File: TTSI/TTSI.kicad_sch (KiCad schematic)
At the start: 34 parts, among them J101 Conn_01x02_Pin, Q101 NMOS, Q102 NMOS, Q103 NMOS, Q104 PMOS, Q105 NMOS, Q106 NMOS, U101 641964-1, U102 641964-1, U103 R-78E5.0-0.5, U104 74AHC1G32, U105 641964-1, U106 74AHC1G08, U107 LM555xM, U108 641964-1

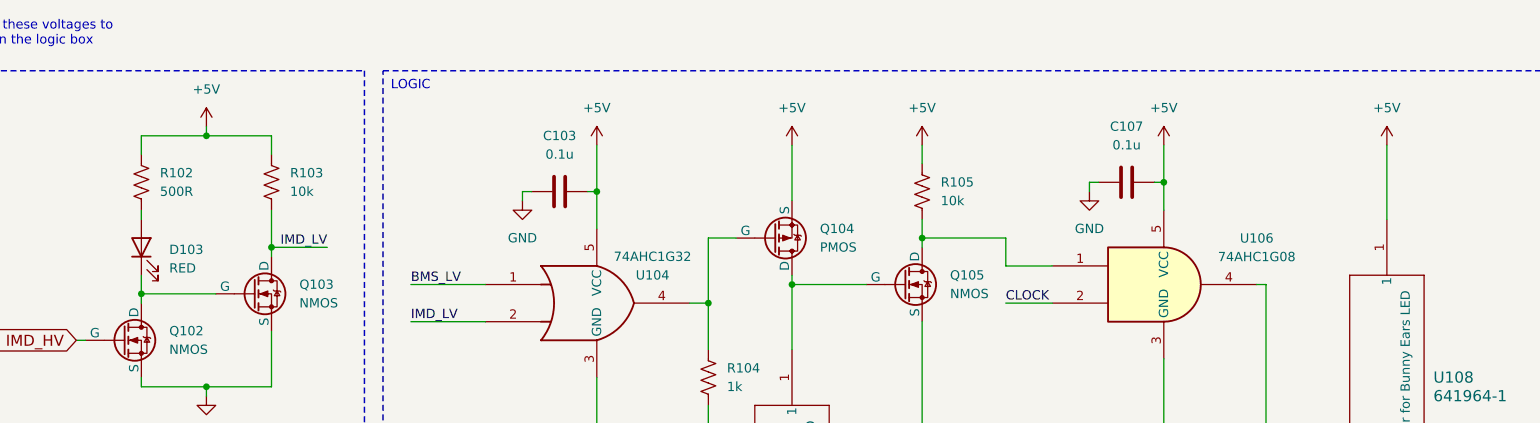
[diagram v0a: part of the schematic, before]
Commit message: Few changes to BOM as well as added 12v to bunny ears
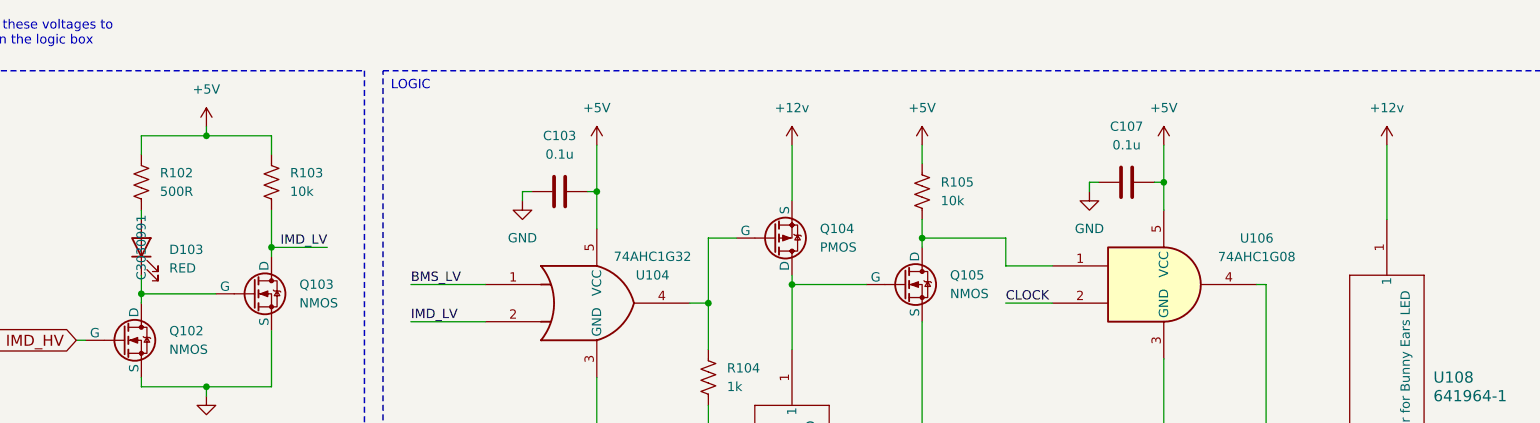
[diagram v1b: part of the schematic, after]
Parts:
- C104: footprint (none) -> Capacitor_SMD:C_0402_1005Metric
- D103: footprint (none) -> LED_SMD:LED_0201_0603Metric; JLC# (none) -> C3030991
- Q101, Q102, Q103, Q105, Q106: footprint (none) -> Package_TO_SOT_SMD:SOT-23
- Q104: footprint (none) -> Package_TO_SOT_SMD:SOT-523
- R101, R102, R103, R104, R105, R106, R107, R108: footprint (none) -> Resistor_SMD:R_0201_0603Metric
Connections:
- net +5V: no longer Q104.3 (S), U108.1
- new net +12v: Q104.3 (S), U108.1
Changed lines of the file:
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@@
 			)
 		)
-		(property "Footprint" ""
+		(property "Footprint" "Resistor_SMD:R_0201_0603Metric"
 			(at 177.546 53.594 90)
 			(effects
@@
 			)
 		)
-		(property "Footprint" ""
+		(property "Footprint" "Package_TO_SOT_SMD:SOT-23"
 			(at 129.54 71.12 0)
 			(effects
@@
 			)
 		)
-		(property "Footprint" ""
+		(property "Footprint" "Resistor_SMD:R_0201_0603Metric"
 			(at 266.446 54.864 90)
 			(effects
@@
 			)
 		)
-		(property "Footprint" ""
+		(property "Footprint" "Resistor_SMD:R_0201_0603Metric"
 			(at 318.516 124.714 90)
 			(effects
@@
 			)
 		)
-		(property "Footprint" ""
+		(property "Footprint" "Resistor_SMD:R_0201_0603Metric"
 			(at 327.914 166.116 90)
 			(effects
@@
 			)
 		)
-		(property "Footprint" ""
+		(property "Footprint" "Package_TO_SOT_SMD:SOT-23"
 			(at 161.29 72.39 0)
 			(effects
@@
 			)
 		)
-		(property "Datasheet" "641964-1"
+		(property "Datasheet" "https://www.te.com/usa-en/product-641964-1.datasheet.pdf"
 			(at 328.93 58.42 0)
 			(effects
@@
 			)
 		)
-		(property "Datasheet" "641964-1"
+		(property "Datasheet" "https://www.te.com/usa-en/product-641964-1.datasheet.pdf"
 			(at 247.65 76.2 0)
 			(effects
@@
 			)
 		)
-		(property "Footprint" ""
+		(property "Footprint" "Package_TO_SOT_SMD:SOT-23"
 			(at 331.47 118.11 0)
 			(effects
@@
 			)
 		)
-		(property "Value" "+5V"
+		(property "Value" "+12v"
 			(at 328.93 43.18 0)
 			(effects
@@
 			)
 		)
-		(property "Footprint" ""
+		(property "Footprint" "Package_TO_SOT_SMD:SOT-523"
 			(at 250.19 63.5 0)
 			(effects
@@
 			)
 		)
-		(property "Footprint" ""
+		(property "Footprint" "Resistor_SMD:R_0201_0603Metric"
 			(at 128.016 58.674 90)
 			(effects
@@
 			)
 		)
-		(property "Footprint" ""
+		(property "Footprint" "Resistor_SMD:R_0201_0603Metric"
 			(at 159.766 53.594 90)
 			(effects
@@
 			)
 		)
-		(property "Footprint" ""
+		(property "Footprint" "Capacitor_SMD:C_0402_1005Metric"
 			(at 278.13 163.83 0)
 			(effects
@@
 			)
 		)
-		(property "Footprint" ""
+		(property "Footprint" "Resistor_SMD:R_0201_0603Metric"
 			(at 237.236 80.264 90)
 			(effects
@@
 			)
 		)
-		(property "Footprint" ""
+		(property "Footprint" "Package_TO_SOT_SMD:SOT-23"
 			(at 179.07 66.04 0)
 			(effects
@@
 			)
 		)
-		(property "Datasheet" "641964-1"
+		(property "Datasheet" "https://www.te.com/usa-en/product-641964-1.datasheet.pdf"
 			(at 30.48 111.76 0)
 			(effects
@@
 			)
 		)
-		(property "Footprint" ""
+		(property "Footprint" "LED_SMD:LED_0201_0603Metric"
 			(at 158.75 62.23 0)
 			(effects
@@
 			)
 		)
-		(property "Datasheet" "~"
+		(property "Datasheet" "https://www.we-online.com/components/products/datasheet/150060RS75000.pdf"
 			(at 158.75 62.23 0)
 			(effects
@@
 			)
 		)
+		(property "JLC#" "C3030991"
+			(at 158.75 62.23 0)
+			(effects
+				(font
+					(size 1.27 1.27)
+				)
+			)
+		)
 		(pin "2"
 		)
@@
 			)
 		)
-		(property "Datasheet" "641964-1"
+		(property "Datasheet" "https://www.te.com/usa-en/product-641964-1.datasheet.pdf"
 			(at 54.61 111.76 0)
 			(effects
@@
 			)
 		)
-		(property "Footprint" ""
+		(property "Footprint" "Package_TO_SOT_SMD:SOT-23"
 			(at 267.97 64.77 0)
 			(effects
@@
 			)
 		)
-		(property "Footprint" ""
+		(property "Footprint" "Resistor_SMD:R_0201_0603Metric"
 			(at 338.074 180.086 90)
 			(effects
@@
 			)
 		)
-		(property "Value" "+5V"
+		(property "Value" "+12v"
 			(at 247.65 43.18 0)
 			(effects

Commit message: R,C values for 555. Layout start
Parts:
- C108: value C -> 22u
- R107: value R_US -> 15k
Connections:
- net +12v: no longer U108.1
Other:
- note added: "Parth 3/21/2025 -Chose values of to make 555 timer at 5Hz. -Removed 12V flag on the bunny ear LED connector after logic gate. Will connect 12V to led directly from harness for now."
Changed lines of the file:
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@@
 		)
 	)
+	(text "Parth 3/21/2025\n-Chose values of  to make 555 timer at 5Hz. \n-Removed 12V flag on the bunny ear LED connector after logic gate. \n	Will connect 12V to led directly from harness for now. \n\n"
+		(exclude_from_sim no)
+		(at 370.332 57.658 0)
+		(effects
+			(font
+				(size 2.54 2.54)
+			)
+			(justify left top)
+		)
+	)
 	(text "Ok these level shifters are shifting these voltages to \n5v for the OR GATE logic seen in the logic box\n"
 		(exclude_from_sim no)
@@
 		)
 	)
-	(text_box "ASTALE 555 - 50% DUTY - 2-5Hz"
+	(text_box "ASTABLE 555 - 50% DUTY - 2-5Hz"
 		(exclude_from_sim no)
 		(at 274.32 143.51 0)
@@
 			)
 		)
-		(property "Value" "R_US"
+		(property "Value" "15k"
 			(at 334.01 166.37 90)
 			(effects
@@
 	)
 	(symbol
-		(lib_name "+5V_1")
-		(lib_id "power:+5V")
-		(at 328.93 48.26 0)
-		(unit 1)
-		(exclude_from_sim no)
-		(in_bom yes)
-		(on_board yes)
-		(dnp no)
-		(fields_autoplaced yes)
-		(property "Reference" "#PWR0127"
-			(at 328.93 52.07 0)
-			(effects
-				(font
-					(size 1.27 1.27)
-				)
-				(hide yes)
-			)
-		)
-		(property "Value" "+12v"
-			(at 328.93 43.18 0)
-			(effects
-				(font
-					(size 1.27 1.27)
-				)
-			)
-		)
-		(property "Footprint" ""
-			(at 328.93 48.26 0)
-			(effects
-				(font
-					(size 1.27 1.27)
-				)
-				(hide yes)
-			)
-		)
-		(property "Datasheet" ""
-			(at 328.93 48.26 0)
-			(effects
-				(font
-					(size 1.27 1.27)
-				)
-				(hide yes)
-			)
-		)
-		(property "Description" "Power symbol creates a global label with name \"+5V\""
-			(at 328.93 48.26 0)
-			(effects
-				(font
-					(size 1.27 1.27)
-				)
-				(hide yes)
-			)
-		)
-		(pin "1"
-		)
-		(instances
-			(project "TTSI 4"
-				(path "/8333e4c5-977f-459c-982e-d2d7d024e7e8"
-					(reference "#PWR0127")
-					(unit 1)
-				)
-			)
-		)
-	)
-	(symbol
 		(lib_id "Simulation_SPICE:PMOS")
 		(at 245.11 60.96 0)
@@
 			)
 		)
-		(property "Value" "C"
+		(property "Value" "22u"
 			(at 342.9 196.8499 0)
 			(effects
@@
 		(on_board yes)
 		(dnp no)
-		(fields_autoplaced yes)
 		(property "Reference" "D103"
 			(at 162.56 62.5474 90)
@@
 		)
 		(property "JLC#" "C3030991"
-			(at 158.75 62.23 0)
+			(at 155.956 61.722 0)
 			(effects
 				(font

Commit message: notes
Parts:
- removed J101: Conn_01x02_Pin, symbol Connector:Conn_01x02_Pin
- U101, U102, U105, U108: footprint 641964-1_TYC -> (none)
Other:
- note added: "Parth 3/21/2025 -Chose values of to make 555 timer at 5Hz. -Removed 12V flag on the bunny ear LED connector after logic gate. Will connect 12V to led directly from harness for now. -Typos -Add symbols properly"
- note removed: "0 - 352.8 V"
- note removed: "Parth 3/21/2025 -Chose values of to make 555 timer at 5Hz. -Removed 12V flag on the bunny ear LED connector after logic gate. Will connect 12V to led directly from harness for now."
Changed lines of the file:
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@@
 		)
 	)
-	(text "0 - 352.8 V"
+	(text "Parth 3/21/2025\n-Chose values of  to make 555 timer at 5Hz. \n-Removed 12V flag on the bunny ear LED connector after logic gate. \n	Will connect 12V to led directly from harness for now. \n-Typos\n-Add symbols properly\n"
 		(exclude_from_sim no)
-		(at 30.734 134.112 90)
-		(effects
-			(font
-				(size 1.27 1.27)
-			)
-		)
-	)
-	(text "Parth 3/21/2025\n-Chose values of  to make 555 timer at 5Hz. \n-Removed 12V flag on the bunny ear LED connector after logic gate. \n	Will connect 12V to led directly from harness for now. \n\n"
-		(exclude_from_sim no)
-		(at 370.332 57.658 0)
+		(at 19.812 211.074 0)
 		(effects
 			(font
@@
 		)
 	)
-	(text "0 - 352.8 V"
-		(exclude_from_sim no)
-		(at 52.324 134.112 90)
-		(effects
-			(font
-				(size 1.27 1.27)
-			)
-		)
-	)
 	(text_box "LEVEL SHIFTERS + IMD LIGHT"
 		(exclude_from_sim no)
@@
 	(text_box "12V\nBMS - ACTIVE LOW\nIMD - ACTIVE HIGH"
 		(exclude_from_sim no)
-		(at 19.05 38.1 0)
+		(at 20.32 38.1 0)
 		(size 82.55 54.61)
 		(margins 1.0541 1.0541 1.0541 1.0541)
@@
 	(text_box "Please enter all mistakes and the how/why did you fix them.\n\n- Find out if bunny ears are +5V or +12V\n\nPCB NOTES\n- Set up constraints according to https://jlcpcb.com/capabilities/pcb-capabilities\n- Remember to set up board edges. Try to use even number like 100x100 or something (Draw lines on edge cuts layer)\n- Bypass caps take priority, place as close as possible to power pins (but not too close)\n- Place regulator close to +12V conn\n- Use power puddles and 0.5mm traces for distriuting power\n- Use 0.3mm traces for signals\n- Place solid uninterrupted GND plane on bottom side\n- Place GND plan on top as well "
 		(exclude_from_sim no)
-		(at 19.05 176.53 0)
+		(at 19.05 172.72 0)
 		(size 124.46 35.56)
 		(margins 0.9525 0.9525 0.9525 0.9525)
@@
 	)
 	(junction
-		(at 62.23 59.69)
-		(diameter 0)
-		(color 0 0 0 0)
-	)
-	(junction
 		(at 314.96 158.75)
 		(diameter 0)
@@
 	)
 	(junction
-		(at 50.8 57.15)
-		(diameter 0)
-		(color 0 0 0 0)
-	)
-	(junction
 		(at 328.93 173.99)
 		(diameter 0)
@@
 	(wire
 		(pts
+			(xy 69.85 57.15) (xy 50.8 57.15)
+		)
+		(stroke
+			(width 0)
+			(type default)
+		)
+	)
+	(wire
+		(pts
 			(xy 284.48 170.18) (xy 284.48 168.91)
 		)
@@
 	(wire
 		(pts
-			(xy 158.75 46.99) (xy 167.64 46.99)
+			(xy 50.8 57.15) (xy 50.8 63.5)
 		)
 		(stroke
@@
 	(wire
 		(pts
-			(xy 276.86 64.77) (xy 283.21 64.77)
+			(xy 158.75 46.99) (xy 167.64 46.99)
 		)
 		(stroke
@@
 	(wire
 		(pts
-			(xy 88.9 107.95) (xy 92.71 107.95)
+			(xy 276.86 64.77) (xy 283.21 64.77)
 		)
 		(stroke
@@
 	(wire
 		(pts
-			(xy 158.75 49.53) (xy 158.75 46.99)
+			(xy 88.9 107.95) (xy 92.71 107.95)
 		)
 		(stroke
@@
 	(wire
 		(pts
-			(xy 50.8 57.15) (xy 50.8 63.5)
+			(xy 158.75 49.53) (xy 158.75 46.99)
 		)
 		(stroke
@@
 	(wire
 		(pts
-			(xy 49.53 57.15) (xy 50.8 57.15)
-		)
-		(stroke
-			(width 0)
-			(type default)
-		)
-	)
-	(wire
-		(pts
 			(xy 289.56 179.07) (xy 302.26 179.07)
 		)
@@
 	(wire
 		(pts
-			(xy 50.8 57.15) (xy 69.85 57.15)
-		)
-		(stroke
-			(width 0)
-			(type default)
-		)
-	)
-	(wire
-		(pts
 			(xy 118.11 73.66) (xy 119.38 73.66)
 		)
@@
 	(wire
 		(pts
-			(xy 49.53 59.69) (xy 62.23 59.69)
-		)
-		(stroke
-			(width 0)
-			(type default)
-		)
-	)
-	(wire
-		(pts
 			(xy 62.23 59.69) (xy 69.85 59.69)
 		)
@@
 			)
 		)
-		(property "Footprint" "641964-1_TYC"
+		(property "Footprint" ""
 			(at 328.93 58.42 0)
 			(effects
@@
 			)
 		)
-		(property "Footprint" "641964-1_TYC"
+		(property "Footprint" ""
 			(at 247.65 76.2 0)
 			(effects
@@
 	)
 	(symbol
-		(lib_id "Connector:Conn_01x02_Pin")
-		(at 44.45 57.15 0)
-		(unit 1)
-		(exclude_from_sim no)
-		(in_bom yes)
-		(on_board yes)
-		(dnp no)
-		(property "Reference" "J101"
-			(at 46.228 54.102 0)
-			(effects
-				(font
-					(size 1.27 1.27)
-				)
-			)
-		)
-		(property "Value" "Conn_01x02_Pin"
-			(at 45.085 54.61 0)
-			(effects
-				(font
-					(size 1.27 1.27)
-				)
-				(hide yes)
-			)
-		)
-		(property "Footprint" ""
-			(at 44.45 57.15 0)
-			(effects
-				(font
-					(size 1.27 1.27)
-				)
-				(hide yes)
-			)
-		)
-		(property "Datasheet" "~"
-			(at 44.45 57.15 0)
-			(effects
-				(font
-					(size 1.27 1.27)
-				)
-				(hide yes)
-			)
-		)
-		(property "Description" "Generic connector, single row, 01x02, script generated"
-			(at 44.45 57.15 0)
-			(effects
-				(font
-					(size 1.27 1.27)
-				)
-				(hide yes)
-			)
-		)
-		(property "JLC#" ""
-			(at 44.45 57.15 0)
-			(effects
-				(font
-					(size 1.27 1.27)
-				)
-				(hide yes)
-			)
-		)
-		(pin "1"
-		)
-		(pin "2"
-		)
-		(instances
-			(project "TTSI 4"
-				(path "/8333e4c5-977f-459c-982e-d2d7d024e7e8"
-					(reference "J101")
-					(unit 1)
-				)
-			)
-		)
-	)
-	(symbol
 		(lib_id "Device:R_US")
 		(at 127 58.42 0)
@@
 			)
 		)
-		(property "Footprint" "641964-1_TYC"
+		(property "Footprint" ""
 			(at 30.48 111.76 0)
 			(effects
@@
 			)
 		)
-		(property "Footprint" "641964-1_TYC"
+		(property "Footprint" ""
 			(at 54.61 111.76 0)
 			(effects
